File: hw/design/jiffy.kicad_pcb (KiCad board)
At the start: 4 copper layers, 110 x 46 mm, 199 parts, among them J1 DX4R005JJ2R1800, J2 RJE72-188-1401, J3 TFM-110-02-S-D-WT, J4 Conn_01x30, J5 Conn_01x30, M1 MHNP_2.5mm, M2 MHNP_2.5mm, M3 MHNP_2.5mm, M4 MHNP_2.5mm, Q1 CSD17313Q2Q1, T1 PT61018PEL, U1 MCIMX6G2AVM07, U10 SN74AHC1G08, U11 LAN8710, U12 USBLC6-4, U13 FAN53541, U14 NCV551SN33T1G, U2 MT41K512M16HA-125, U3 LP3470M5-3.08, U4 FAN53541, U5 FAN5355UC00, U6 FEMC004GTTE7-T13-17, U7 USBLC6-4, U8 NCP360SNAET1G, U9 LM74610, X1 NX2012SA-32.768K-STD-MUB-1, X2 NX2520SA-24.000000MHZ

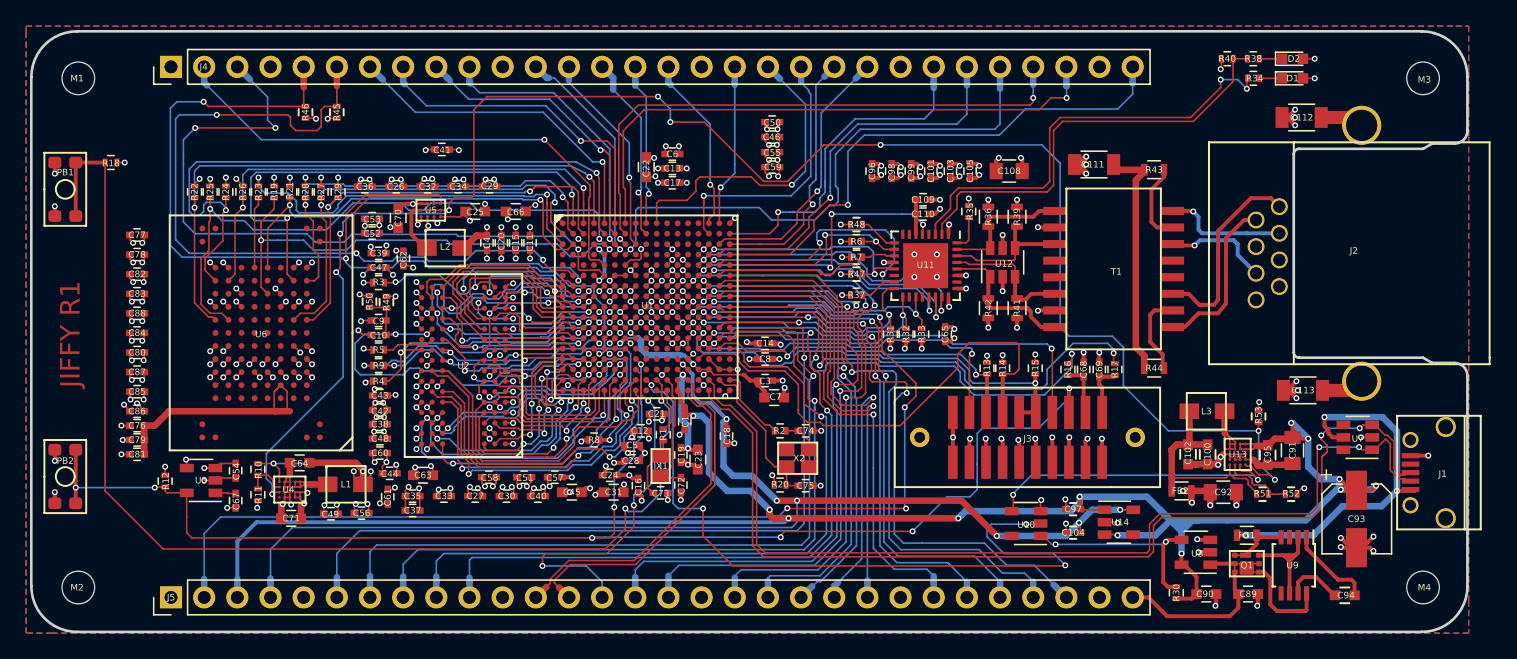
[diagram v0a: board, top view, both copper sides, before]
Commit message: Migrate design to current KiCad format
Convert the legacy schematics and project to .kicad_sch/.kicad_pro,
update the board file, and add the legacy cache library to the
symbol library table.
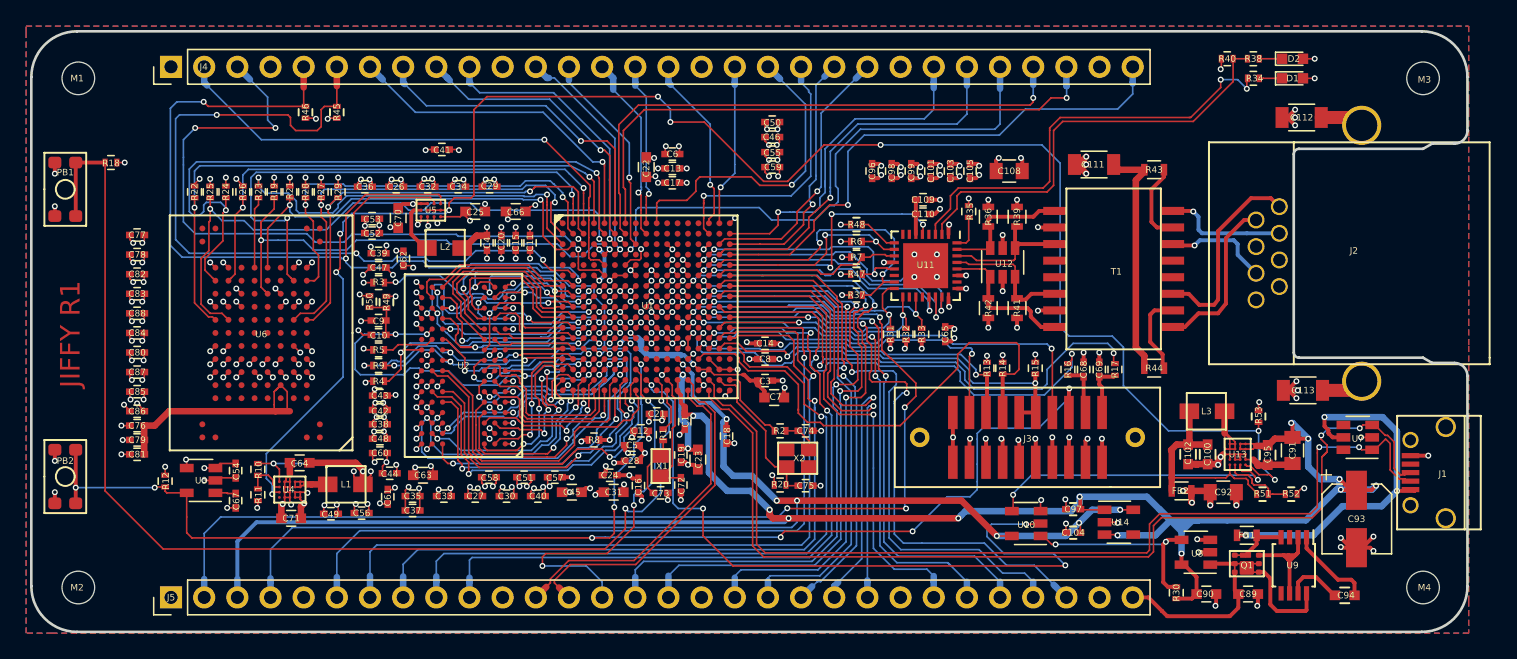
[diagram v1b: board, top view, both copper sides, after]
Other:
- net class Default removed
- net class Eth removed
